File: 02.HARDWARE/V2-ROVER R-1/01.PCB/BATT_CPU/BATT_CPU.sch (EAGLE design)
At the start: 85 parts, among them J1 DF40C_2.0_-20DS-0.4V_51_, Q1 BSS84W-7-F, Q2 BSS84W-7-F, Q3 2N7002PW, Q4 2N7002PW, Q5 BSS84W-7-F, U1 ATSAMD21G18_QFN, U3 TPS78230DDCR, U6 MAX9062EUK+T, U8 SN74LVC1G19DBVR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

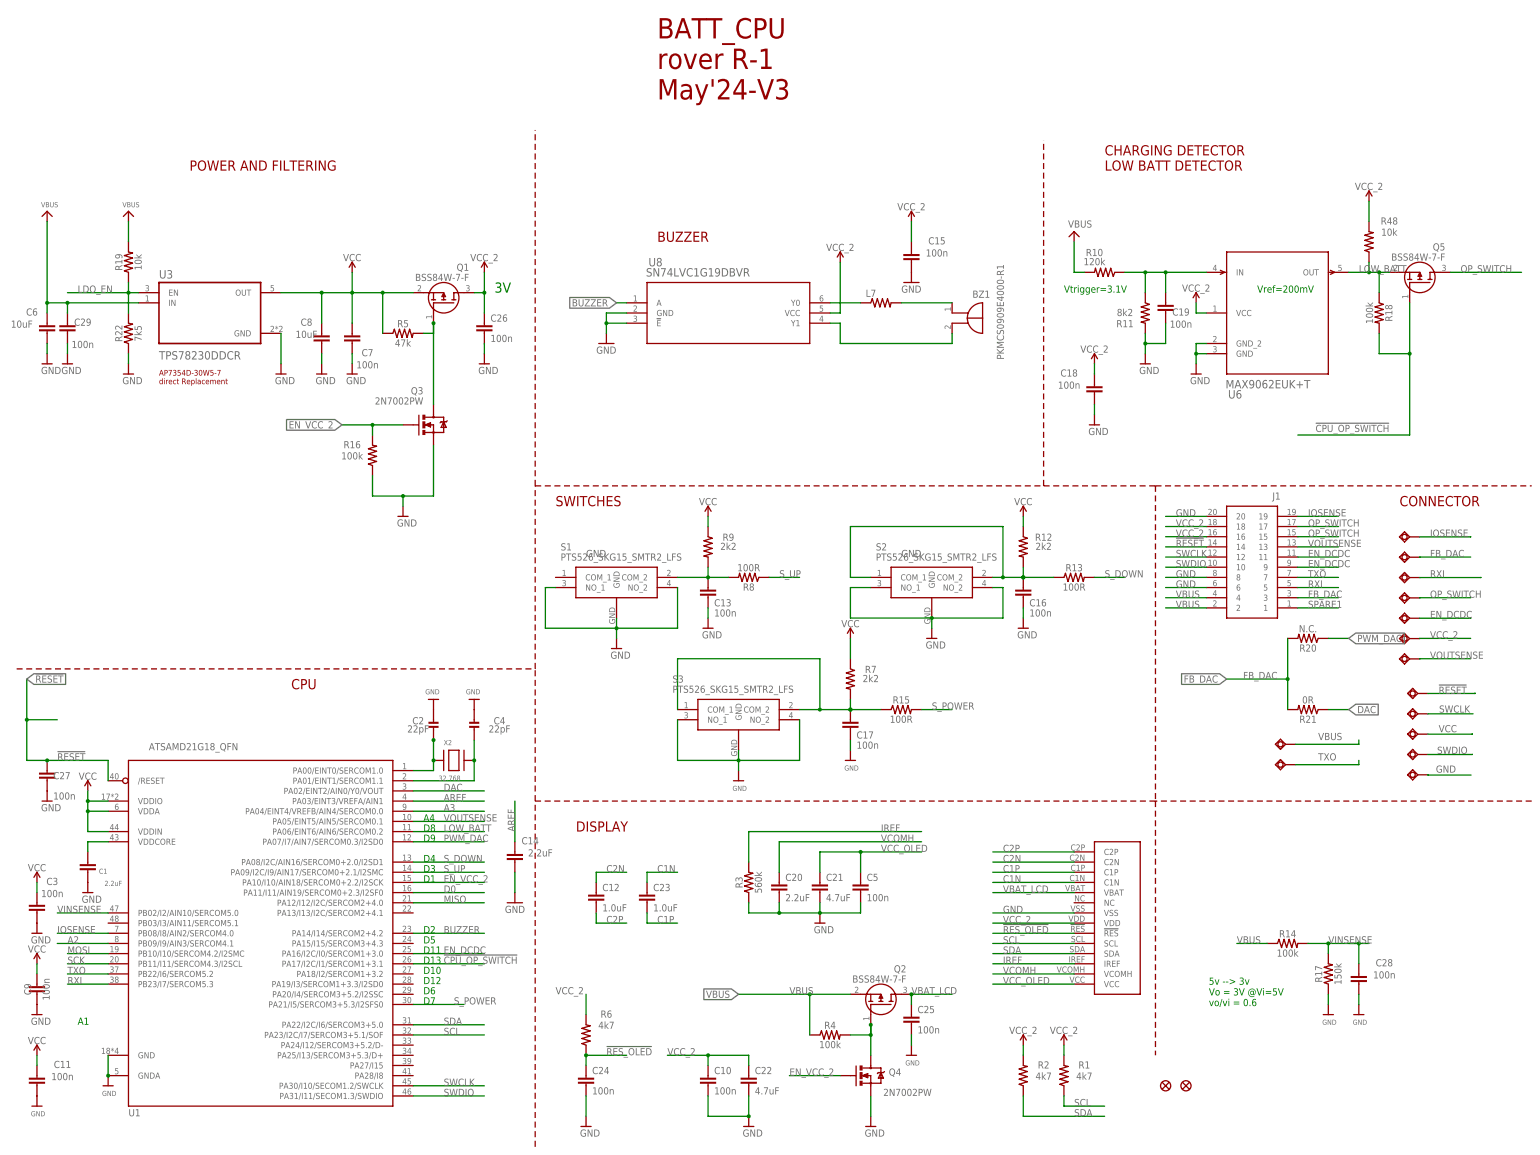
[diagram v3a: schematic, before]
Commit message: Cambios menores en esquematico
Se corrigen valores de Resistencias para PWM
Actualizado el titulo del esquematico
Limpieza general
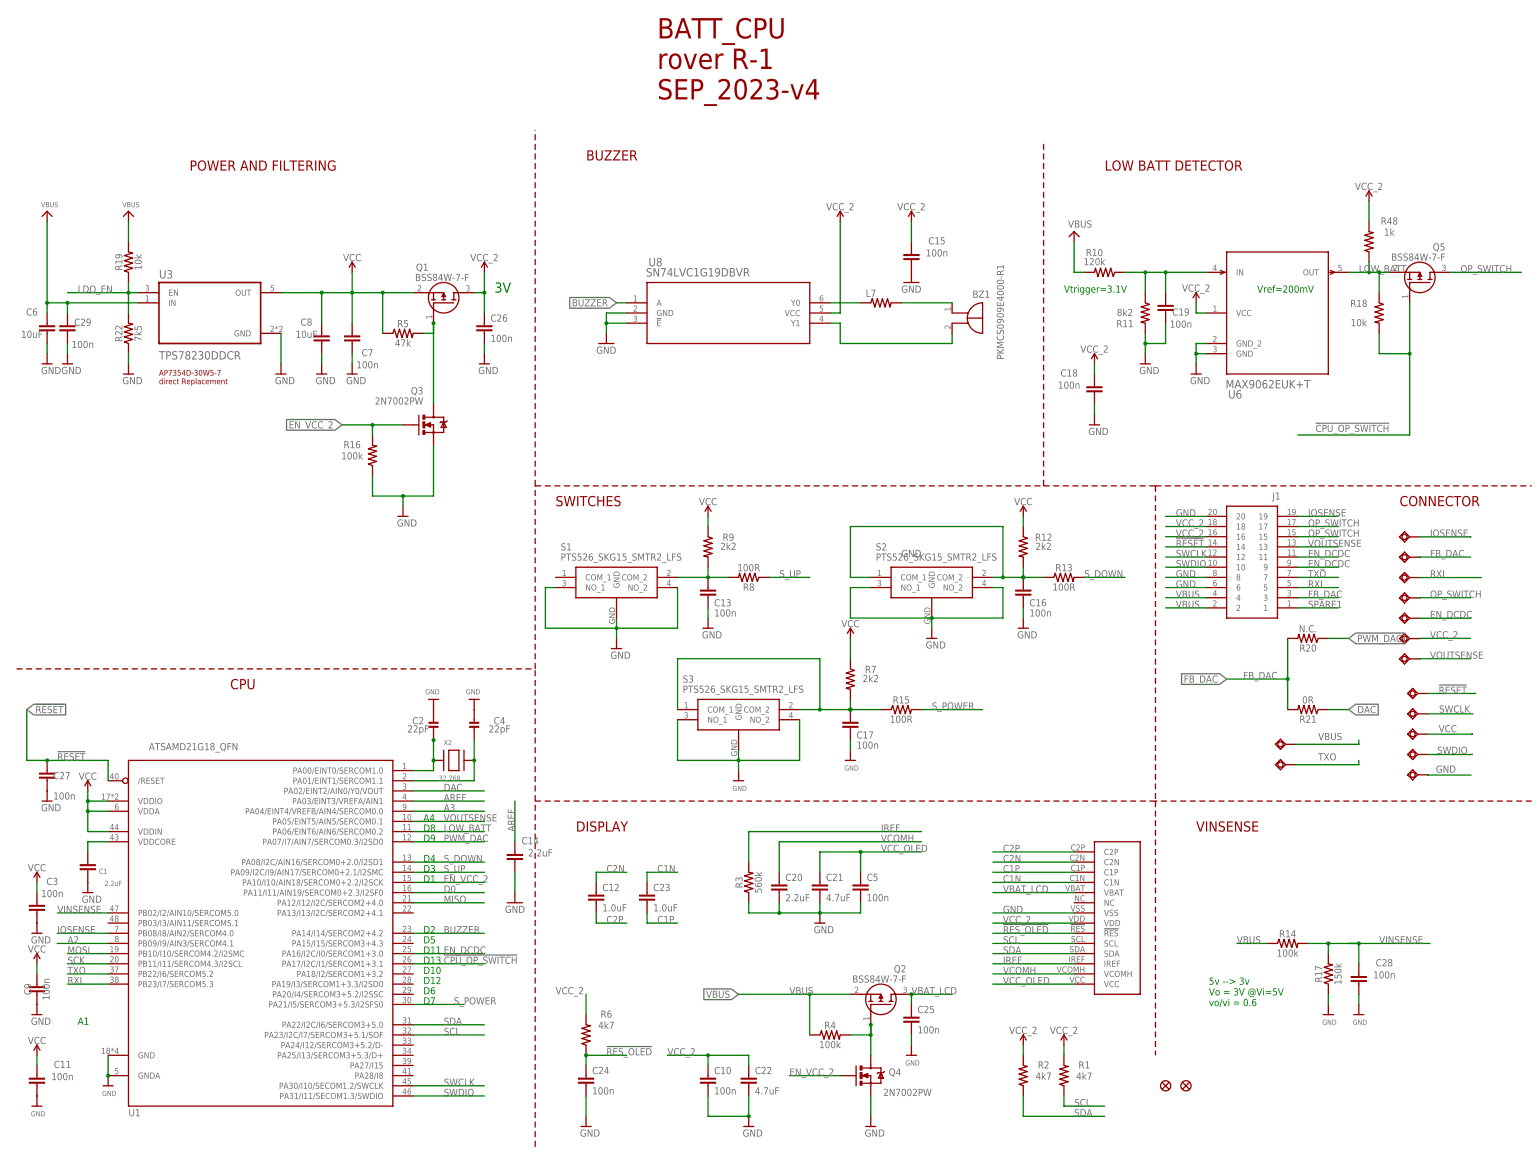
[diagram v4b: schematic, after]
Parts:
- R18: value 100k -> 10k
- R48: value 10k -> 1k
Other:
- note added: "BATT_CPU rover R-1 SEP_2023-v4"
- note added: "LOW BATT DETECTOR"
- note added: "VINSENSE"
- note removed: "BATT_CPU rover R-1 May'24-V3"
- note removed: "CHARGING DETECTOR LOW BATT DETECTOR"
- moved on the sheet: R13
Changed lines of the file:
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@@
 <part name="U$30" library="OLED 66 64x48" deviceset="64X32_OLED_049" device=""/>
 <part name="C19" library="SparkFun-Capacitors" library_urn="urn:adsk.eagle:library:510" deviceset="0.1UF" device="-0402-16V-10%" package3d_urn="urn:adsk.eagle:package:37413/1" value="100n"/>
-<part name="R48" library="SparkFun-Resistors" library_urn="urn:adsk.eagle:library:532" deviceset="RESISTOR" device="0402" package3d_urn="urn:adsk.eagle:package:39657/1" value="10k"/>
+<part name="R48" library="SparkFun-Resistors" library_urn="urn:adsk.eagle:library:532" deviceset="RESISTOR" device="0402" package3d_urn="urn:adsk.eagle:package:39657/1" value="1k"/>
 <part name="Q1" library="BSS84W-7-F" deviceset="BSS84W-7-F" device=""/>
 <part name="R5" library="SparkFun-Resistors" library_urn="urn:adsk.eagle:library:532" deviceset="RESISTOR" device="0402" package3d_urn="urn:adsk.eagle:package:39657/1" value="47k"/>
@@
 <part name="SUPPLY11" library="SparkFun-PowerSymbols" deviceset="VCC" device="" value="VCC_2"/>
 <part name="Q5" library="BSS84W-7-F" deviceset="BSS84W-7-F" device=""/>
-<part name="R18" library="SparkFun-Resistors" library_urn="urn:adsk.eagle:library:532" deviceset="RESISTOR" device="0402" package3d_urn="urn:adsk.eagle:package:39657/1" value="100k"/>
+<part name="R18" library="SparkFun-Resistors" library_urn="urn:adsk.eagle:library:532" deviceset="RESISTOR" device="0402" package3d_urn="urn:adsk.eagle:package:39657/1" value="10k"/>
 <part name="U$31" library="microbuilder" deviceset="GND" device=""/>
 <part name="C27" library="SparkFun-Capacitors" library_urn="urn:adsk.eagle:library:510" deviceset="0.1UF" device="-0402-16V-10%" package3d_urn="urn:adsk.eagle:package:37413/1" value="100n"/>
@@
 <wire x1="134.62" y1="167.64" x2="134.62" y2="256.54" width="0.1524" layer="94" style="shortdash"/>
 <wire x1="289.56" y1="88.9" x2="134.62" y2="88.9" width="0.1524" layer="94" style="shortdash"/>
-<text x="165.1" y="228.6" size="2.54" layer="94">BUZZER</text>
+<text x="147.32" y="248.92" size="2.54" layer="94">BUZZER</text>
 <text x="40.64" y="193.04" size="1.4224" layer="94">AP7354D-30W5-7
 direct Replacement</text>
@@
 <text x="20.32" y="33.02" size="1.778" layer="91">A1</text>
 <wire x1="134.62" y1="167.64" x2="261.62" y2="167.64" width="0.1524" layer="94" style="shortdash"/>
-<text x="276.86" y="246.38" size="2.54" layer="94">CHARGING DETECTOR
-LOW BATT DETECTOR</text>
-<text x="73.66" y="116.84" size="2.54" layer="94">CPU</text>
+<text x="276.86" y="246.38" size="2.54" layer="94">LOW BATT DETECTOR</text>
+<text x="58.42" y="116.84" size="2.54" layer="94">CPU</text>
 <wire x1="261.62" y1="167.64" x2="289.56" y2="167.64" width="0.1524" layer="94" style="shortdash"/>
 <wire x1="289.56" y1="167.64" x2="383.54" y2="167.64" width="0.1524" layer="94" style="shortdash"/>
@@
 <text x="165.1" y="264.16" size="5.08" layer="94">BATT_CPU
 rover R-1
-May'24-V3</text>
+SEP_2023-v4</text>
 <text x="144.78" y="81.28" size="2.54" layer="94">DISPLAY</text>
 <text x="139.7" y="162.56" size="2.54" layer="94">SWITCHES</text>
 <text x="350.52" y="162.56" size="2.54" layer="94">CONNECTOR</text>
 <wire x1="383.54" y1="88.9" x2="289.56" y2="88.9" width="0.1524" layer="94" style="shortdash"/>
+<text x="299.72" y="81.28" size="2.54" layer="94">VINSENSE</text>
 </plain>
 <instances>
 <instance part="C6" gate="G$1" x="12.7" y="205.74" smashed="yes">
 <attribute name="NAME" x="8.91" y="211.07" size="1.778" layer="95" font="vector" ratio="7" rot="R180" align="center"/>
-<attribute name="VALUE" x="6.37" y="208.04" size="1.778" layer="96" font="vector" ratio="7" rot="R180" align="center"/>
+<attribute name="VALUE" x="8.91" y="205.5" size="1.778" layer="96" font="vector" ratio="7" rot="R180" align="center"/>
 </instance>
 <instance part="U$27" gate="G$1" x="12.7" y="198.12" smashed="yes">
@@
 </instance>
 <instance part="S3" gate="G$1" x="170.18" y="111.76" smashed="yes">
-<attribute name="NAME" x="168.91" y="119.38" size="1.778" layer="95" align="center-left"/>
-<attribute name="VALUE" x="168.91" y="116.84" size="1.778" layer="96" align="center-left"/>
+<attribute name="NAME" x="171.45" y="119.38" size="1.778" layer="95" align="center-left"/>
+<attribute name="VALUE" x="171.45" y="116.84" size="1.778" layer="96" align="center-left"/>
 </instance>
 <instance part="U$13" gate="G$1" x="185.42" y="93.98" smashed="yes">
@@
 <attribute name="VALUE" x="261.62" y="153.416" size="1.778" layer="96" font="vector" ratio="7" align="top-center"/>
 </instance>
-<instance part="R13" gate="G$1" x="269.24" y="144.78" smashed="yes">
-<attribute name="NAME" x="269.24" y="146.304" size="1.778" layer="95" font="vector" ratio="7" align="bottom-center"/>
-<attribute name="VALUE" x="269.24" y="143.256" size="1.778" layer="96" font="vector" ratio="7" align="top-center"/>
+<instance part="R13" gate="G$1" x="266.7" y="144.78" smashed="yes">
+<attribute name="NAME" x="266.7" y="146.304" size="1.778" layer="95" font="vector" ratio="7" align="bottom-center"/>
+<attribute name="VALUE" x="266.7" y="143.256" size="1.778" layer="96" font="vector" ratio="7" align="top-center"/>
 </instance>
 <instance part="SUPPLY6" gate="G$1" x="177.8" y="160.02" smashed="yes">
@@
 </instance>
 <instance part="Q1" gate="G$1" x="109.22" y="208.28" smashed="yes" rot="MR90">
-<attribute name="NAME" x="118.11" y="222.25" size="1.778" layer="95" rot="MR0" align="center-left"/>
+<attribute name="NAME" x="107.95" y="222.25" size="1.778" layer="95" rot="MR0" align="center-left"/>
 <attribute name="VALUE" x="118.11" y="219.71" size="1.778" layer="96" rot="MR0" align="center-left"/>
 </instance>
@@
 <attribute name="VALUE" x="213.36" y="132.334" size="1.778" layer="96" align="bottom-center"/>
 </instance>
-<instance part="SUPPLY15" gate="G$1" x="210.82" y="223.52" smashed="yes">
-<attribute name="VALUE" x="210.82" y="226.314" size="1.778" layer="96" align="bottom-center"/>
+<instance part="SUPPLY15" gate="G$1" x="210.82" y="233.68" smashed="yes">
+<attribute name="VALUE" x="210.82" y="236.474" size="1.778" layer="96" align="bottom-center"/>
 </instance>
 <instance part="SUPPLY16" gate="G$1" x="228.6" y="233.68" smashed="yes">
@@
 </instance>
 <instance part="R18" gate="G$1" x="345.44" y="210.82" smashed="yes" rot="R270">
-<attribute name="NAME" x="346.964" y="210.82" size="1.778" layer="95" font="vector" ratio="7" rot="R270" align="bottom-center"/>
-<attribute name="VALUE" x="343.916" y="210.82" size="1.778" layer="96" font="vector" ratio="7" rot="R270" align="top-center"/>
+<attribute name="NAME" x="340.36" y="212.344" size="1.778" layer="95" font="vector" ratio="7" align="bottom-center"/>
+<attribute name="VALUE" x="340.36" y="209.296" size="1.778" layer="96" font="vector" ratio="7" align="top-center"/>
 </instance>
 <instance part="U$31" gate="G$1" x="147.32" y="7.62" smashed="yes">
@@
 <pinref part="S1" gate="G$1" pin="GND"/>
 <wire x1="154.94" y1="134.62" x2="154.94" y2="132.08" width="0.1524" layer="91"/>
-<label x="147.32" y="149.86" size="1.778" layer="95"/>
 <pinref part="U$19" gate="G$1" pin="GND"/>
 <pinref part="S1" gate="G$1" pin="NO_1"/>
@@
 <junction x="12.7" y="99.06"/>
 <wire x1="12.7" y1="99.06" x2="7.62" y2="99.06" width="0.1524" layer="91"/>
-<wire x1="7.62" y1="99.06" x2="7.62" y2="109.22" width="0.1524" layer="91"/>
-<label x="7.62" y="119.38" size="1.778" layer="95" xref="yes"/>
-<wire x1="7.62" y1="109.22" x2="7.62" y2="119.38" width="0.1524" layer="91"/>
-<wire x1="15.24" y1="109.22" x2="7.62" y2="109.22" width="0.1524" layer="91"/>
-<junction x="7.62" y="109.22"/>
+<label x="7.62" y="111.76" size="1.778" layer="95" xref="yes"/>
+<wire x1="7.62" y1="99.06" x2="7.62" y2="111.76" width="0.1524" layer="91"/>
 </segment>
 <segment>
@@
 <segment>
 <pinref part="R8" gate="G$1" pin="1"/>
-<wire x1="193.04" y1="144.78" x2="200.66" y2="144.78" width="0.1524" layer="91"/>
+<wire x1="193.04" y1="144.78" x2="203.2" y2="144.78" width="0.1524" layer="91"/>
 <label x="195.58" y="144.78" size="1.778" layer="95"/>
 </segment>
@@
 <segment>
 <pinref part="R13" gate="G$1" pin="2"/>
-<wire x1="274.32" y1="144.78" x2="281.94" y2="144.78" width="0.1524" layer="91"/>
-<label x="276.86" y="144.78" size="1.778" layer="95"/>
+<wire x1="271.78" y1="144.78" x2="281.94" y2="144.78" width="0.1524" layer="91"/>
+<label x="271.78" y="144.78" size="1.778" layer="95"/>
 </segment>
 </net>
@@
 <wire x1="332.74" y1="53.34" x2="340.36" y2="53.34" width="0.1524" layer="91"/>
 <junction x="332.74" y="53.34"/>
-<label x="332.74" y="53.34" size="1.778" layer="95"/>
+<label x="345.44" y="53.34" size="1.778" layer="95"/>
 <pinref part="C28" gate="G$1" pin="1"/>
-<wire x1="340.36" y1="53.34" x2="342.9" y2="53.34" width="0.1524" layer="91"/>
+<wire x1="340.36" y1="53.34" x2="358.14" y2="53.34" width="0.1524" layer="91"/>
 <wire x1="340.36" y1="48.26" x2="340.36" y2="53.34" width="0.1524" layer="91"/>
 <wire x1="337.82" y1="53.34" x2="340.36" y2="53.34" width="0.1524" layer="91"/>
@@
 <wire x1="256.54" y1="144.78" x2="256.54" y2="147.32" width="0.1524" layer="91"/>
 <pinref part="R13" gate="G$1" pin="1"/>
-<wire x1="256.54" y1="144.78" x2="264.16" y2="144.78" width="0.1524" layer="91"/>
+<wire x1="256.54" y1="144.78" x2="261.62" y2="144.78" width="0.1524" layer="91"/>
 <junction x="256.54" y="144.78"/>
 <junction x="256.54" y="144.78"/>
@@
 <segment>
 <pinref part="R15" gate="G$1" pin="2"/>
-<wire x1="231.14" y1="111.76" x2="238.76" y2="111.76" width="0.1524" layer="91"/>
+<wire x1="231.14" y1="111.76" x2="246.38" y2="111.76" width="0.1524" layer="91"/>
 <label x="233.68" y="111.76" size="1.778" layer="95"/>
 </segment>
@@
 <pinref part="U8" gate="A" pin="VCC"/>
 <wire x1="208.28" y1="210.82" x2="210.82" y2="210.82" width="0.1524" layer="91"/>
-<wire x1="210.82" y1="210.82" x2="210.82" y2="223.52" width="0.1524" layer="91"/>
+<wire x1="210.82" y1="210.82" x2="210.82" y2="233.68" width="0.1524" layer="91"/>
 <pinref part="SUPPLY15" gate="G$1" pin="VCC"/>
 </segment>

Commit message: Fix error
Solucion de inconsistencia de valores entre el BRD y el SCH
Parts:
- R5: value 47k -> 100k
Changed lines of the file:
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@@
 <part name="R48" library="SparkFun-Resistors" library_urn="urn:adsk.eagle:library:532" deviceset="RESISTOR" device="0402" package3d_urn="urn:adsk.eagle:package:39657/1" value="1k"/>
 <part name="Q1" library="BSS84W-7-F" deviceset="BSS84W-7-F" device=""/>
-<part name="R5" library="SparkFun-Resistors" library_urn="urn:adsk.eagle:library:532" deviceset="RESISTOR" device="0402" package3d_urn="urn:adsk.eagle:package:39657/1" value="47k"/>
+<part name="R5" library="SparkFun-Resistors" library_urn="urn:adsk.eagle:library:532" deviceset="RESISTOR" device="0402" package3d_urn="urn:adsk.eagle:package:39657/1" value="100k"/>
 <part name="U$1" library="microbuilder" deviceset="GND" device=""/>
 <part name="Q3" library="SparkFun-DiscreteSemi" deviceset="MOSFET-NCHANNEL" device="2N7002PW" value="2N7002PW"/>

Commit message: Adiccion de Fiducidiales y actualizacion de Version
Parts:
- added FD_1, FD_2, FD_3, FD_4, FD_5: FD_1, testpad:TPTP06SQ
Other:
- note added: "BATT_CPU rover R-1 Nov'23 v5"
- note removed: "BATT_CPU rover R-1 SEP_2023-v4"
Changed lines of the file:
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@@
 <part name="R22" library="SparkFun-Resistors" library_urn="urn:adsk.eagle:library:532" deviceset="RESISTOR" device="0402" package3d_urn="urn:adsk.eagle:package:39657/1" value="7k5"/>
 <part name="U$39" library="microbuilder" deviceset="GND" device=""/>
+<part name="FD_1" library="testpad" library_urn="urn:adsk.eagle:library:385" deviceset="TP" device="TP06SQ" package3d_urn="urn:adsk.eagle:package:27952/1" value="FD_1"/>
+<part name="FD_2" library="testpad" library_urn="urn:adsk.eagle:library:385" deviceset="TP" device="TP06SQ" package3d_urn="urn:adsk.eagle:package:27952/1" value="FD_1"/>
+<part name="FD_3" library="testpad" library_urn="urn:adsk.eagle:library:385" deviceset="TP" device="TP06SQ" package3d_urn="urn:adsk.eagle:package:27952/1" value="FD_1"/>
+<part name="FD_4" library="testpad" library_urn="urn:adsk.eagle:library:385" deviceset="TP" device="TP06SQ" package3d_urn="urn:adsk.eagle:package:27952/1" value="FD_1"/>
+<part name="FD_5" library="testpad" library_urn="urn:adsk.eagle:library:385" deviceset="TP" device="TP06SQ" package3d_urn="urn:adsk.eagle:package:27952/1" value="FD_1"/>
 </parts>
 <sheets>
@@
 <text x="165.1" y="264.16" size="5.08" layer="94">BATT_CPU
 rover R-1
-SEP_2023-v4</text>
+Nov'23 v5</text>
 <text x="144.78" y="81.28" size="2.54" layer="94">DISPLAY</text>
 <text x="139.7" y="162.56" size="2.54" layer="94">SWITCHES</text>
@@
 <attribute name="VALUE" x="31.496" y="193.04" size="1.778" layer="96"/>
 </instance>
+<instance part="FD_1" gate="G$1" x="312.42" y="15.24" smashed="yes">
+<attribute name="NAME" x="311.15" y="16.51" size="1.778" layer="95"/>
+<attribute name="TP_SIGNAL_NAME" x="313.69" y="13.97" size="1.778" layer="97"/>
+</instance>
+<instance part="FD_2" gate="G$1" x="320.04" y="15.24" smashed="yes">
+<attribute name="NAME" x="318.77" y="16.51" size="1.778" layer="95"/>
+<attribute name="TP_SIGNAL_NAME" x="321.31" y="13.97" size="1.778" layer="97"/>
+</instance>
+<instance part="FD_3" gate="G$1" x="327.66" y="15.24" smashed="yes">
+<attribute name="NAME" x="326.39" y="16.51" size="1.778" layer="95"/>
+<attribute name="TP_SIGNAL_NAME" x="328.93" y="13.97" size="1.778" layer="97"/>
+</instance>
+<instance part="FD_4" gate="G$1" x="322.58" y="10.16" smashed="yes">
+<attribute name="NAME" x="321.31" y="11.43" size="1.778" layer="95"/>
+<attribute name="TP_SIGNAL_NAME" x="323.85" y="8.89" size="1.778" layer="97"/>
+</instance>
+<instance part="FD_5" gate="G$1" x="330.2" y="10.16" smashed="yes">
+<attribute name="NAME" x="328.93" y="11.43" size="1.778" layer="95"/>
+<attribute name="TP_SIGNAL_NAME" x="331.47" y="8.89" size="1.778" layer="97"/>
+</instance>
 </instances>

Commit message: Salto del compardor en arranques de alguna maquinas. #86
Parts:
- R11: value 8k2 -> 11k
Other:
- note added: "BATT_CPU rover R-1 v6-Sep'24"
- note removed: "BATT_CPU rover R-1 Nov'23 v5"
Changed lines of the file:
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@@
 <part name="U$18" library="microbuilder" deviceset="GND" device=""/>
 <part name="R10" library="SparkFun-Resistors" library_urn="urn:adsk.eagle:library:532" deviceset="RESISTOR" device="0402" package3d_urn="urn:adsk.eagle:package:39657/1" value="120k"/>
-<part name="R11" library="SparkFun-Resistors" library_urn="urn:adsk.eagle:library:532" deviceset="RESISTOR" device="0402" package3d_urn="urn:adsk.eagle:package:39657/1" value="8k2"/>
+<part name="R11" library="SparkFun-Resistors" library_urn="urn:adsk.eagle:library:532" deviceset="RESISTOR" device="0402" package3d_urn="urn:adsk.eagle:package:39657/1" value="11k"/>
 <part name="U$21" library="microbuilder" deviceset="GND" device=""/>
 <part name="U$22" library="microbuilder" deviceset="VBUS" device=""/>
@@
 <text x="165.1" y="264.16" size="5.08" layer="94">BATT_CPU
 rover R-1
-Nov'23 v5</text>
+v6-Sep'24</text>
 <text x="144.78" y="81.28" size="2.54" layer="94">DISPLAY</text>
 <text x="139.7" y="162.56" size="2.54" layer="94">SWITCHES</text>
